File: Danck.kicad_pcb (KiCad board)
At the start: 2 copper layers, 228.6 x 76.2 mm, 125 parts, among them P1 Pad, P2 Pad, P3 Pad, P4 Pad, SW1 SW_PUSH, U1 ProMicro

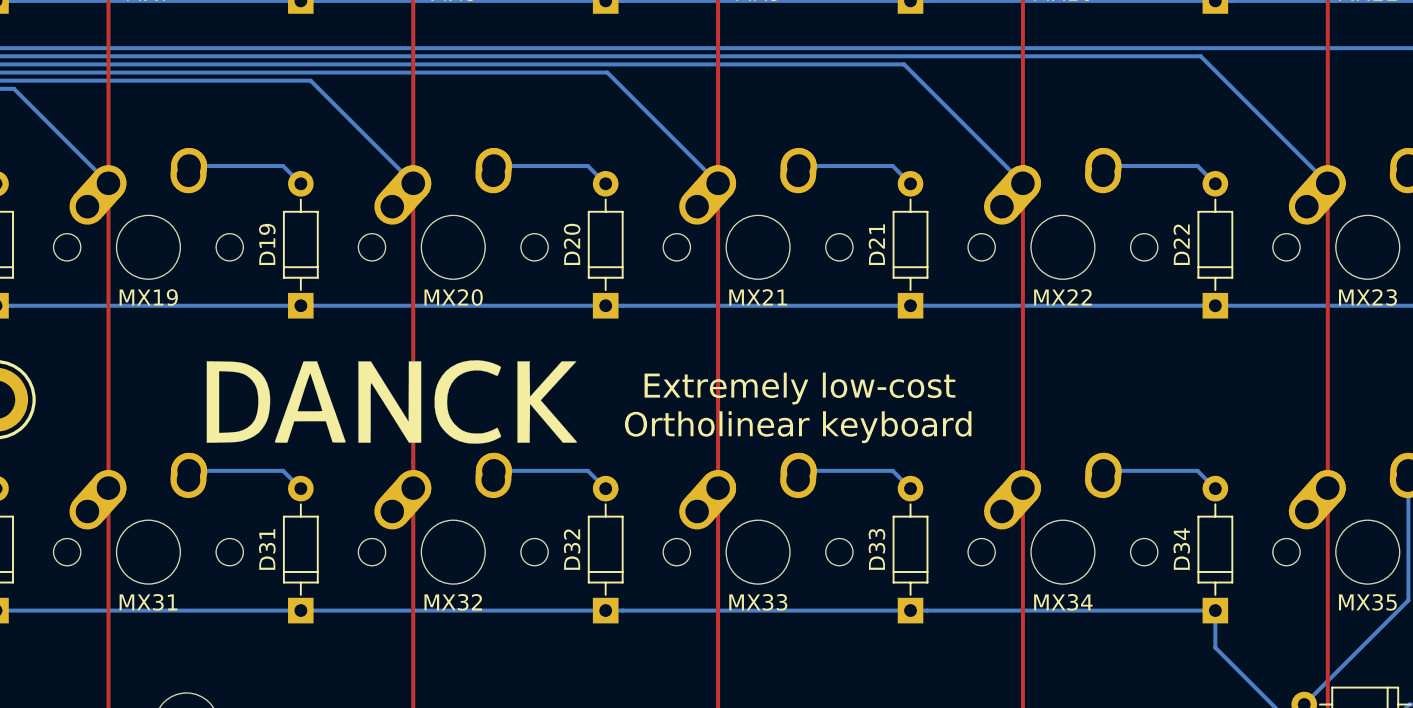
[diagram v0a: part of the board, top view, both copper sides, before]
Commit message: Update footprints for silk
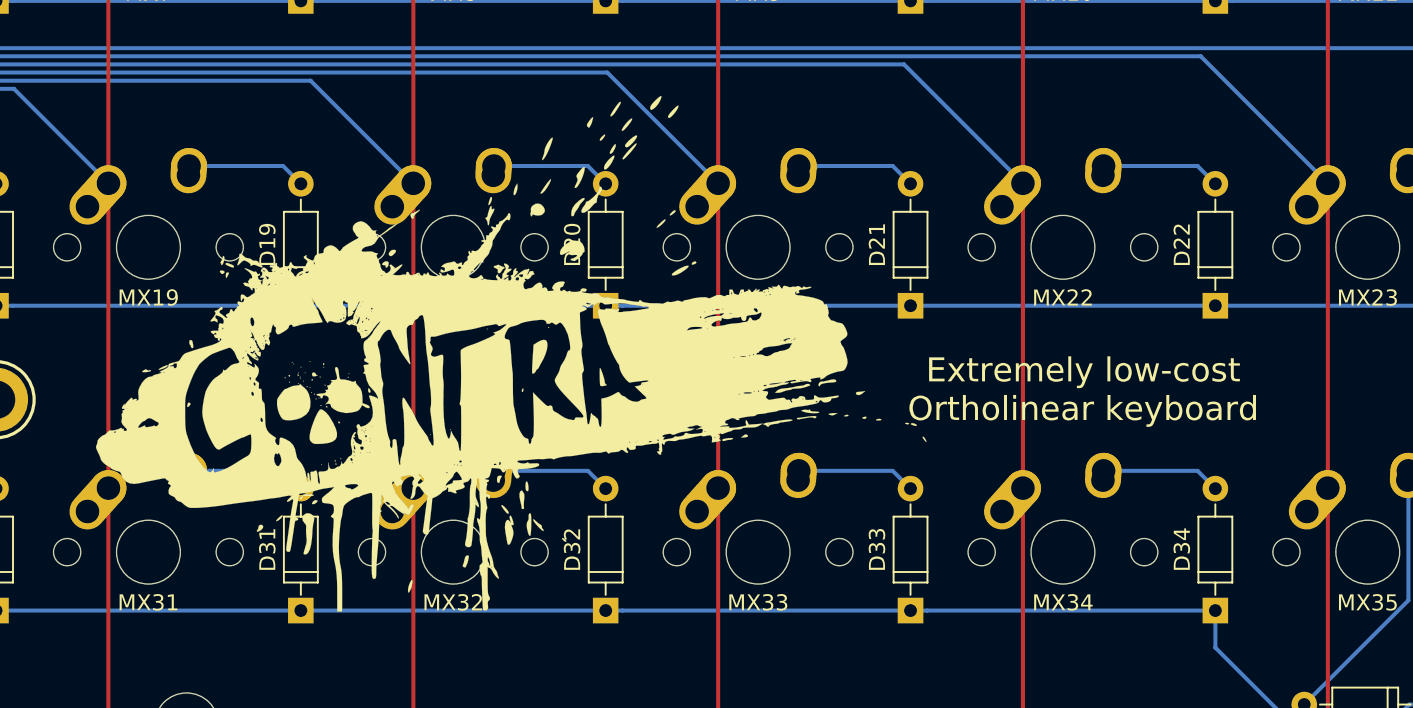
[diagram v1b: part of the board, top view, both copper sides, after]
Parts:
- removed the G*** at (167.5, 66.7)
- added G***: LOGO, memelogo:contra, F.Cu at (175.1, 63.8)
- moved G*** 78.2 mm to (134.6, 53.3)
- moved G*** 61.4 mm to (71.1, 86.4)
- moved G*** 47.9 mm to (88.9, 94.0)
- moved G*** 40.0 mm to (108.0, 58.4)
- moved G*** 23.0 mm to (90.2, 71.1)
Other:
- board text added: "CONTRA"
- board text removed: "DANCK"

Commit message: Reposition memes, add you won't download...
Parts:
- added G***: LOGO, memelogo:youwat, B.Cu at (160.0, 67.3)
- moved G*** 101.6 mm to (45.7, 87.6)
- moved G*** 32.6 mm to (166.4, 97.8)
- moved G*** 25.9 mm to (58.4, 63.5)
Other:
- board text added: "CAUTION: Toxic Memes. DO NOT EAT"
- board text added: "Pro Micro here! Component side faces away from the PCB. Rev 1.4"
- board text removed: "CAUTION Toxic Memes DO NOT EAT"
- board text removed: "Pro Micro here! Component side faces away from the PCB. Rev 1.2"

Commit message: New gerbers
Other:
- board text added: "criminally cheap ortho"
- board text removed: "Hella cheap ortho"
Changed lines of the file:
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@@
 (kicad_pcb (version 4) (host pcbnew 4.0.6)
   (general
-    (links 0)
+    (links 252)
     (no_connects 0)
     (area 28.499999 28.499999 257.250001 104.850001)
@@
   )
   (gr_line (start 100.0125 28.575) (end 257.175 75.40625) (layer B.SilkS) (width 1))
-  (gr_text "Hella cheap ortho" (at 240.50625 63.119) (layer B.SilkS)
+  (gr_text "criminally cheap\northo" (at 238.76 64.77) (layer B.SilkS)
     (effects (font (size 2 2) (thickness 0.4) italic) (justify mirror))
   )

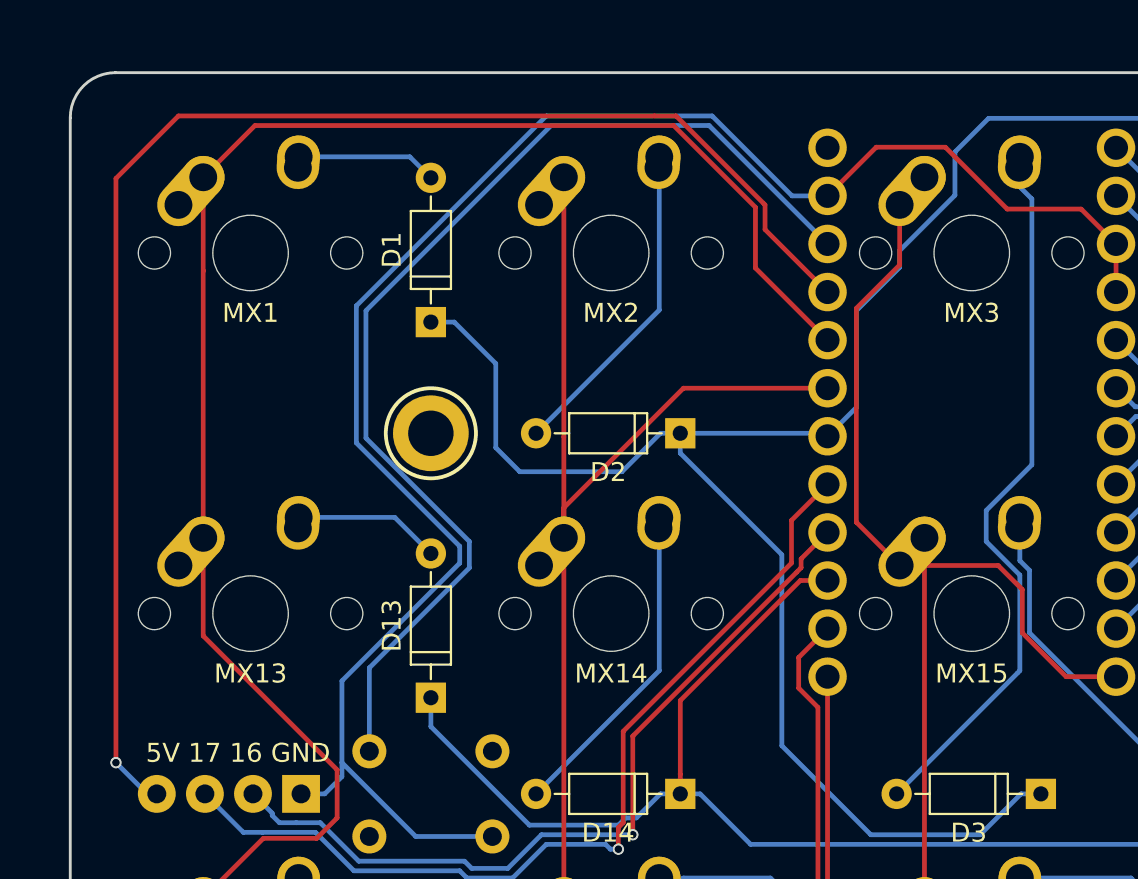
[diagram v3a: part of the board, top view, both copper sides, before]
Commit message: Improve routing, add broken image
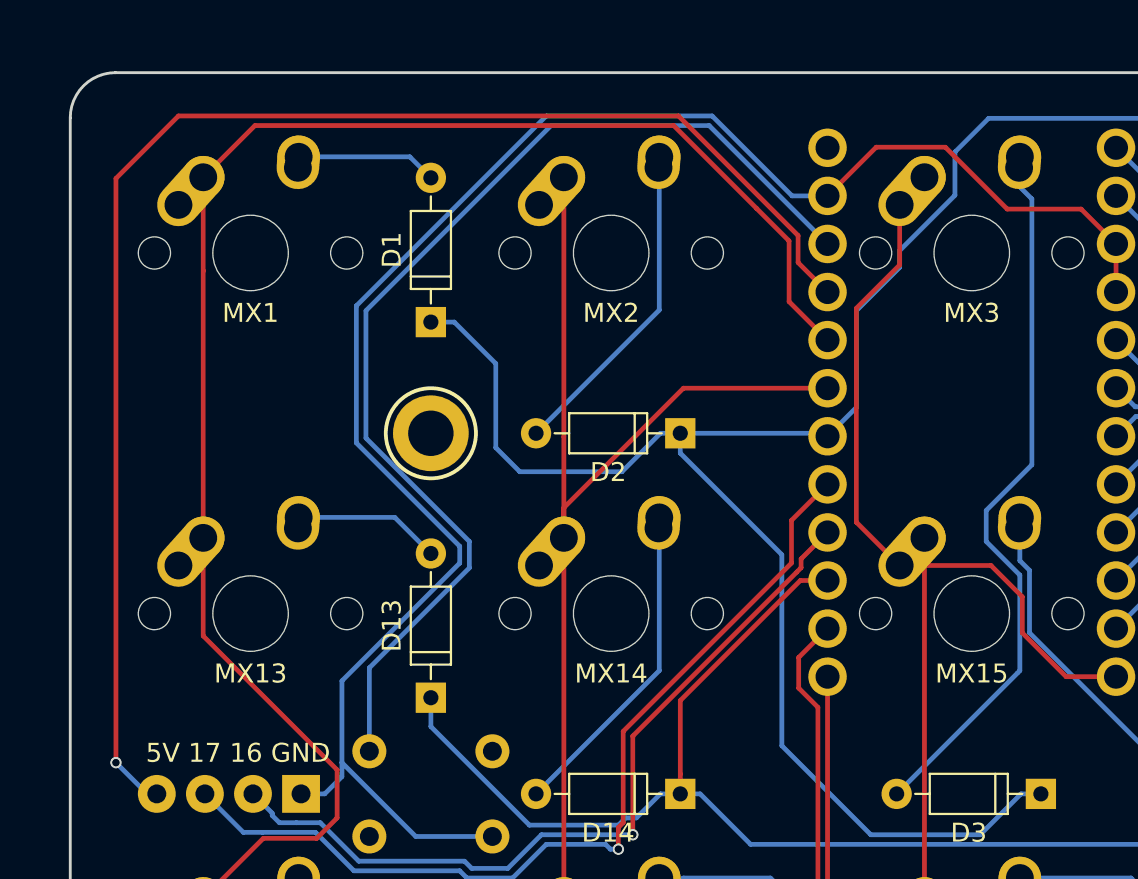
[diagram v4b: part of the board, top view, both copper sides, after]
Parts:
- removed the G*** at (180.7, 83.4)
- added G***: LOGO, memelogo:broken, B.Cu at (186.9, 82.2)

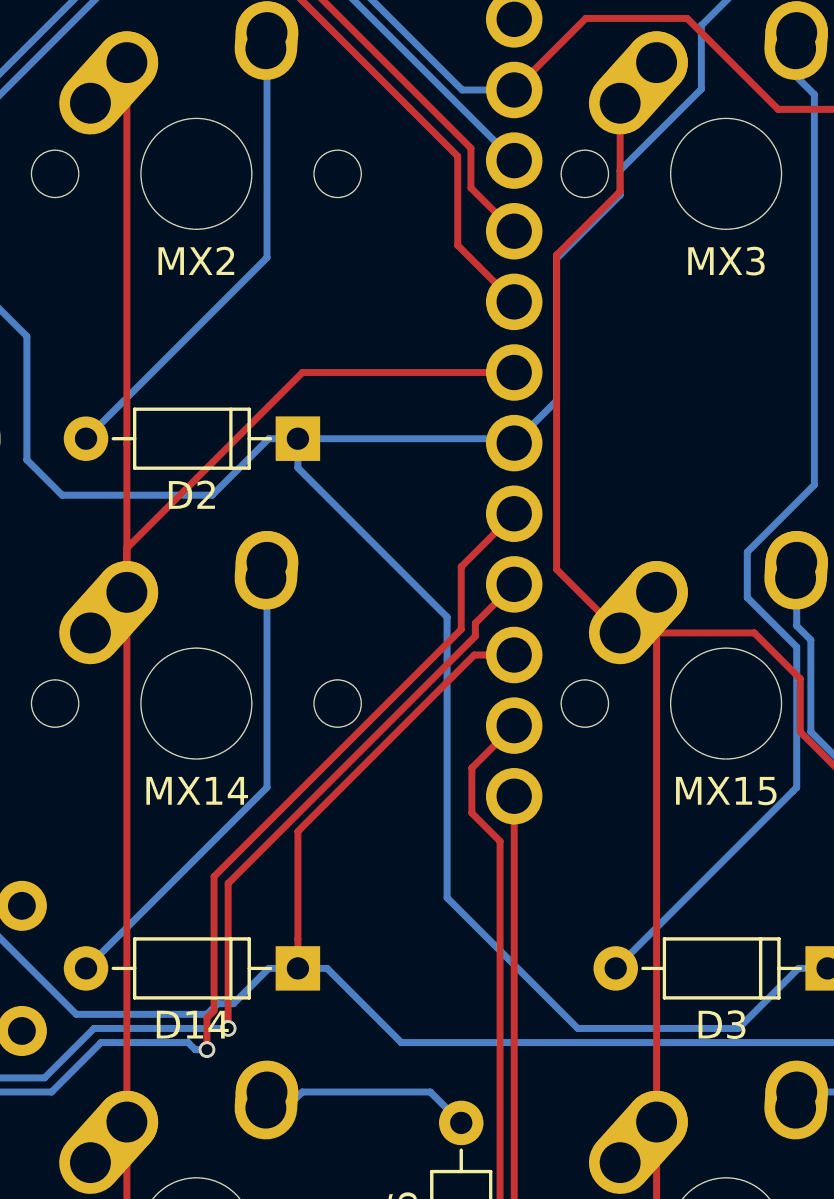
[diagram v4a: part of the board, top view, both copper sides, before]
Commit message: Update some routing
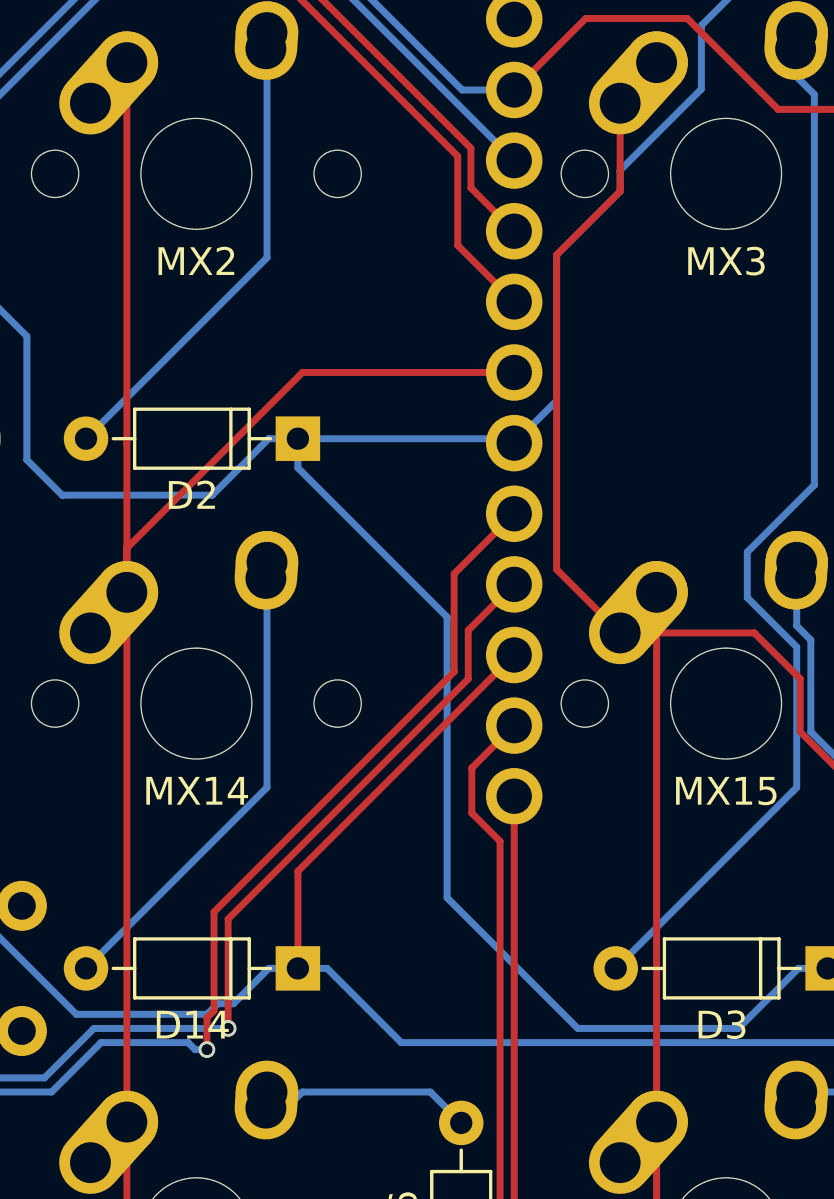
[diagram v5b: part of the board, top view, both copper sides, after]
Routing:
- net ROW1: track 233.6 -> 232.7 mm
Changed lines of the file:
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@@
     (thickness 1.6)
     (drawings 37)
-    (tracks 468)
+    (tracks 466)
     (zones 0)
     (modules 126)
@@
   (segment (start 104.775 41.75125) (end 91.91625 41.75125) (width 0.25) (layer B.Cu) (net 1))
   (segment (start 91.91625 41.75125) (end 87.503 37.338) (width 0.25) (layer B.Cu) (net 1))
-  (segment (start 72.39 37.973) (end 72.39 38.862) (width 0.25) (layer B.Cu) (net 1))
-  (segment (start 87.503 37.338) (end 87.503 32.385) (width 0.25) (layer B.Cu) (net 1))
   (segment (start 87.503 32.385) (end 86.106 30.988) (width 0.25) (layer B.Cu) (net 1))
+  (segment (start 87.503 37.338) (end 87.503 32.385) (width 0.25) (layer B.Cu) (net 1))
+  (segment (start 75.311 35.052) (end 72.39 37.973) (width 0.25) (layer B.Cu) (net 1))
   (segment (start 86.106 30.988) (end 77.089 30.988) (width 0.25) (layer B.Cu) (net 1))
-  (segment (start 75.311 32.766) (end 75.311 35.052) (width 0.25) (layer B.Cu) (net 1))
   (segment (start 77.089 30.988) (end 75.311 32.766) (width 0.25) (layer B.Cu) (net 1))
-  (segment (start 75.311 35.052) (end 72.39 37.973) (width 0.25) (layer B.Cu) (net 1))
-  (segment (start 72.39 38.862) (end 70.104 41.148) (width 0.25) (layer B.Cu) (net 1))
-  (segment (start 70.104 41.148) (end 70.104 46.25975) (width 0.25) (layer B.Cu) (net 1))
+  (segment (start 75.311 32.766) (end 75.311 35.052) (width 0.25) (layer B.Cu) (net 1))
+  (segment (start 72.39 37.973) (end 72.39 38.735) (width 0.25) (layer B.Cu) (net 1))
+  (segment (start 72.39 38.735) (end 70.104 41.021) (width 0.25) (layer B.Cu) (net 1))
   (segment (start 70.104 46.25975) (end 68.58 47.78375) (width 0.25) (layer B.Cu) (net 1))
+  (segment (start 70.104 41.021) (end 70.104 46.25975) (width 0.25) (layer B.Cu) (net 1))
   (segment (start 47.625 41.75125) (end 48.86325 41.75125) (width 0.25) (layer B.Cu) (net 1))
   (segment (start 48.86325 41.75125) (end 51.054 43.942) (width 0.25) (layer B.Cu) (net 1))
@@
   (segment (start 250.19 33.02) (end 250.19 41.11625) (width 0.25) (layer B.Cu) (net 13))
   (segment (start 250.19 41.11625) (end 243.68125 47.625) (width 0.25) (layer B.Cu) (net 13))
+  (segment (start 68.58 55.40375) (end 60.80125 63.1825) (width 0.25) (layer F.Cu) (net 14))
+  (segment (start 60.80125 63.1825) (end 60.80125 66.675) (width 0.25) (layer F.Cu) (net 14))
   (segment (start 60.80125 66.675) (end 59.75125 66.675) (width 0.25) (layer B.Cu) (net 14))
   (segment (start 47.625 63.119) (end 47.625 61.595) (width 0.25) (layer B.Cu) (net 14))
@@
   (segment (start 98.90125 65.625) (end 103.725 60.80125) (width 0.25) (layer B.Cu) (net 14))
   (segment (start 103.725 60.80125) (end 104.775 60.80125) (width 0.25) (layer B.Cu) (net 14))
-  (segment (start 68.58 55.40375) (end 67.14316 55.40375) (width 0.25) (layer F.Cu) (net 14))
-  (segment (start 67.14316 55.40375) (end 60.80125 61.74566) (width 0.25) (layer F.Cu) (net 14))
-  (segment (start 60.80125 61.74566) (end 60.80125 65.625) (width 0.25) (layer F.Cu) (net 14))
-  (segment (start 60.80125 65.625) (end 60.80125 66.675) (width 0.25) (layer F.Cu) (net 14))
   (segment (start 40.64 52.07) (end 45.72 52.07) (width 0.25) (layer B.Cu) (net 15))
   (segment (start 45.72 52.07) (end 47.625 53.975) (width 0.25) (layer B.Cu) (net 15))
@@
   (segment (start 32.639 66.675) (end 33.147 66.675) (width 0.25) (layer B.Cu) (net 68))
   (via (at 30.988 65.024) (size 0.6) (drill 0.4) (layers F.Cu B.Cu) (net 68))
+  (segment (start 68.58 50.32375) (end 66.421 52.48275) (width 0.25) (layer F.Cu) (net 69))
+  (segment (start 66.421 52.48275) (end 66.421 56.007) (width 0.25) (layer F.Cu) (net 69))
+  (segment (start 66.421 56.007) (end 57.785 64.643) (width 0.25) (layer F.Cu) (net 69))
+  (segment (start 57.785 64.643) (end 57.785 68.199) (width 0.25) (layer F.Cu) (net 69))
+  (segment (start 57.785 68.199) (end 57.531 68.453) (width 0.25) (layer F.Cu) (net 69))
+  (segment (start 57.531 68.453) (end 57.531 69.596) (width 0.25) (layer F.Cu) (net 69))
   (segment (start 38.735 68.707) (end 37.719 68.707) (width 0.25) (layer B.Cu) (net 69))
   (segment (start 37.719 68.707) (end 35.687 66.675) (width 0.25) (layer B.Cu) (net 69))
@@
   (segment (start 57.531 69.596) (end 57.106736 69.596) (width 0.25) (layer B.Cu) (net 69))
   (segment (start 57.106736 69.596) (end 56.852736 69.342) (width 0.25) (layer B.Cu) (net 69))
-  (segment (start 57.785 68.199) (end 57.531 68.453) (width 0.25) (layer F.Cu) (net 69))
-  (segment (start 57.531 68.453) (end 57.531 69.596) (width 0.25) (layer F.Cu) (net 69))
   (via (at 57.531 69.596) (size 0.6) (drill 0.4) (layers F.Cu B.Cu) (net 69))
-  (segment (start 57.785 63.373) (end 57.785 68.199) (width 0.25) (layer F.Cu) (net 69))
-  (segment (start 66.675 54.483) (end 57.785 63.373) (width 0.25) (layer F.Cu) (net 69))
-  (segment (start 66.675 52.22875) (end 66.675 54.483) (width 0.25) (layer F.Cu) (net 69))
-  (segment (start 68.58 50.32375) (end 66.675 52.22875) (width 0.25) (layer F.Cu) (net 69))
+  (segment (start 68.58 52.86375) (end 66.929 54.51475) (width 0.25) (layer F.Cu) (net 70))
+  (segment (start 58.293 64.897) (end 58.293 65.659) (width 0.25) (layer F.Cu) (net 70))
+  (segment (start 66.929 54.51475) (end 66.929 56.261) (width 0.25) (layer F.Cu) (net 70))
+  (segment (start 66.929 56.261) (end 58.293 64.897) (width 0.25) (layer F.Cu) (net 70))
+  (segment (start 58.293 65.659) (end 58.293 68.834) (width 0.25) (layer F.Cu) (net 70))
   (segment (start 39.243 67.818) (end 39.243 67.691) (width 0.25) (layer B.Cu) (net 70))
   (segment (start 39.243 67.691) (end 38.227 66.675) (width 0.25) (layer B.Cu) (net 70))
@@
   (segment (start 49.784 70.612) (end 51.689 70.612) (width 0.25) (layer B.Cu) (net 70))
   (segment (start 51.689 70.612) (end 53.467 68.834) (width 0.25) (layer B.Cu) (net 70))
-  (segment (start 66.956759 54.953741) (end 58.293 63.6175) (width 0.25) (layer F.Cu) (net 70))
-  (segment (start 58.293 63.6175) (end 58.293 68.834) (width 0.25) (layer F.Cu) (net 70))
   (via (at 58.293 68.834) (size 0.6) (drill 0.4) (layers F.Cu B.Cu) (net 70))
-  (segment (start 67.183 54.26075) (end 67.183 54.7275) (width 0.25) (layer F.Cu) (net 70))
-  (segment (start 67.183 54.7275) (end 66.956759 54.953741) (width 0.25) (layer F.Cu) (net 70))
-  (segment (start 68.58 52.86375) (end 67.183 54.26075) (width 0.25) (layer F.Cu) (net 70))
   (zone (net 67) (net_name GND) (layer F.Cu) (hatch edge 0.508)
     (connect_pads (clearance 0.381))

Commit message: Remove some artworkr
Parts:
- removed the G*** at (43.2, 46.6)
- removed the G*** at (117.5, 82.5)

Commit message: Add de wey
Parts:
- added G***: LOGO, memelogo:wey, B.Cu at (43.6, 51.9)
- moved G*** 49.3 mm to (102.6, 85.3)
- moved G*** 41.5 mm to (61.5, 62.9)
- moved G*** 29.4 mm to (141.4, 82.4)
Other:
- board text added: "CAUTION: Toxic Memes. DO NOT EAT. Do not wash with beer."
- board text removed: "CAUTION: Toxic Memes. DO NOT EAT"
